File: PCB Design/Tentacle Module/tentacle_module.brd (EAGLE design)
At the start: 101.6 x 30.5 mm, 57 parts, among them IC1 OKR-T/10-W12, IC2 MC7805BDTRKG, IC3 UA78M33CKVU, T1 NTD5867NL, T2 NTD5867NL, T3 NTD5867NL, T4 NTD5867NL, X3 RJ45-8X, X5 RJ45-8X

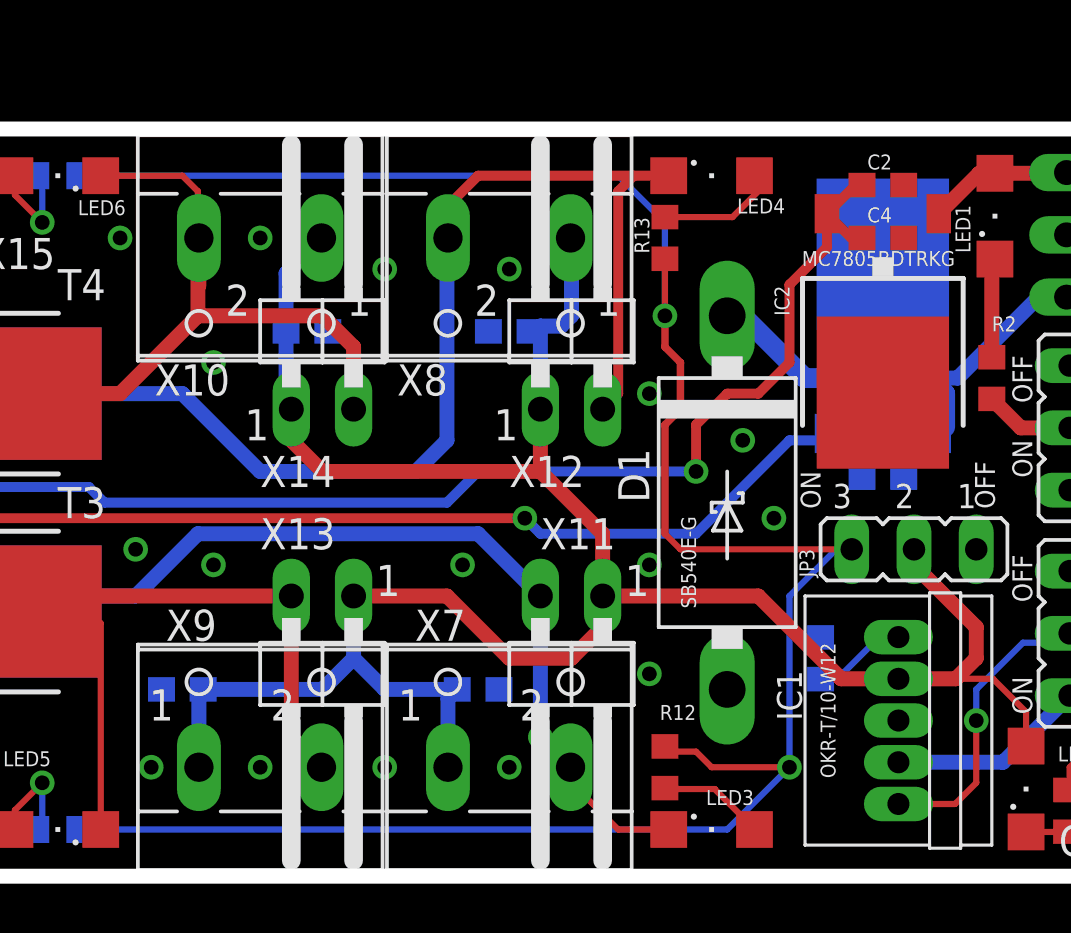
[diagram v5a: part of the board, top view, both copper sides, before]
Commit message: Changed 10uF caps package to 1206
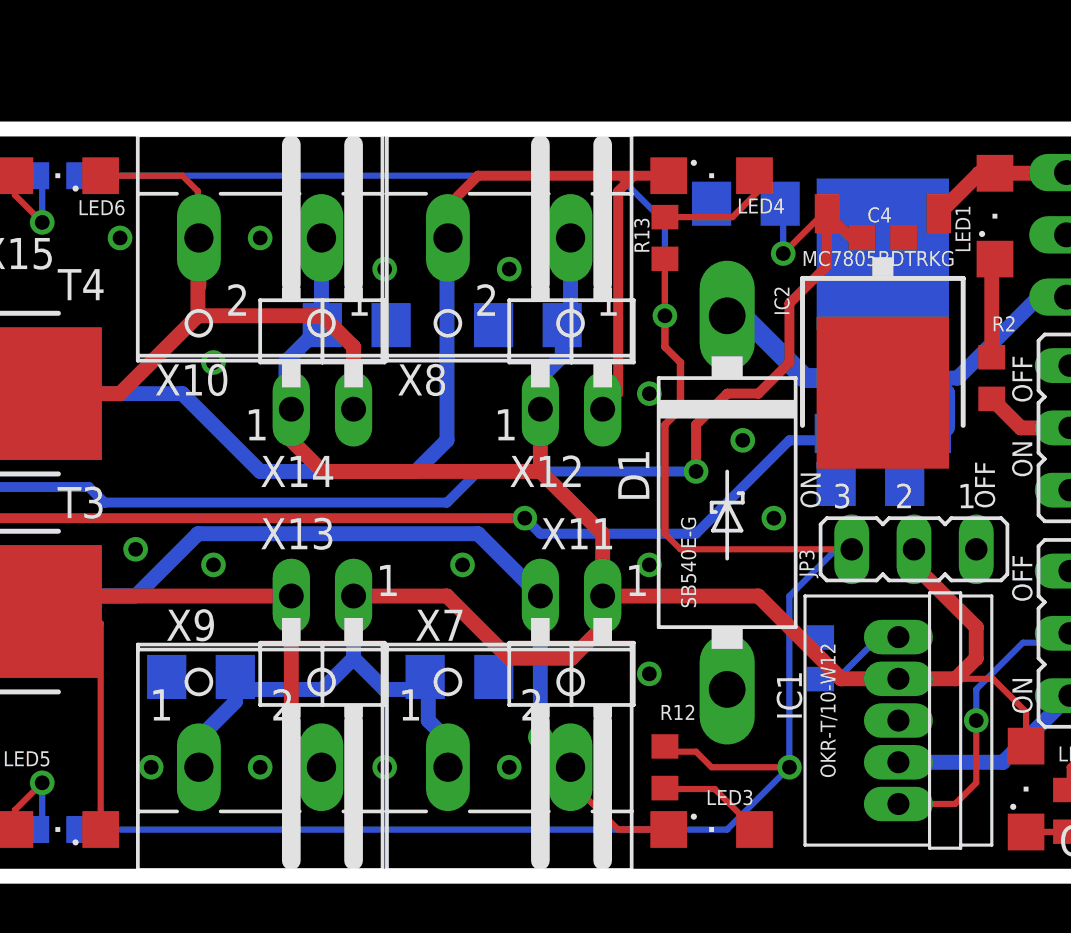
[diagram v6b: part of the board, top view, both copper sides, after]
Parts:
- C2, C3, C6, C7, C8, C9: device rcl:C0603 -> rcl:C1206
- moved C2 5.64 mm to (77.0, 27.4), flipped to the bottom
- moved C9 2.05 mm to (61.1, 22.5)
- moved C6 0.92 mm to (65.3, 8.13)
- moved C8 0.92 mm to (54.7, 8.13)
- moved C7 0.80 mm to (68.1, 22.5)
- moved C3 0.57 mm to (82.0, 16.0)
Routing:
- net +5V: track 101.6 -> 104.3 mm, vias 1 -> 2
- net +3.3V: track 69.9 -> 71.3 mm
- net +5V_HI-PWR: track 100.0 -> 98.5 mm

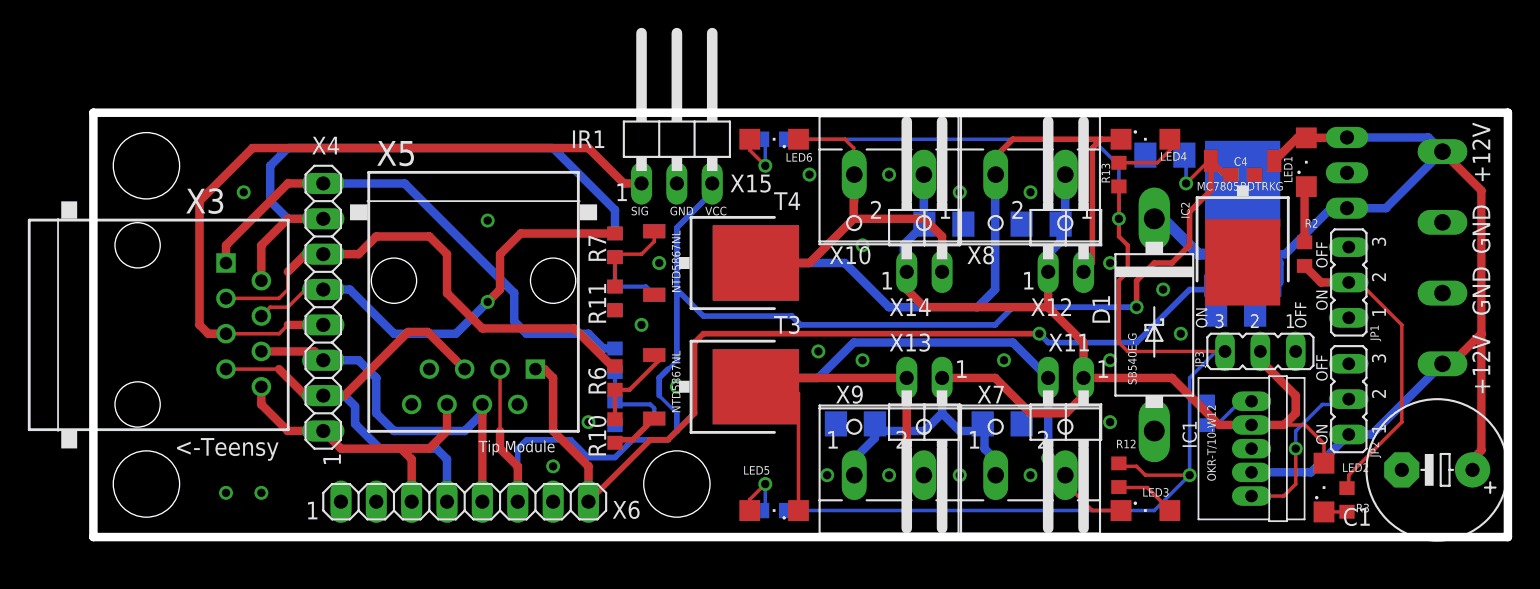
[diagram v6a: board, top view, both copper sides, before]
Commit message: Added labels to silkscreen
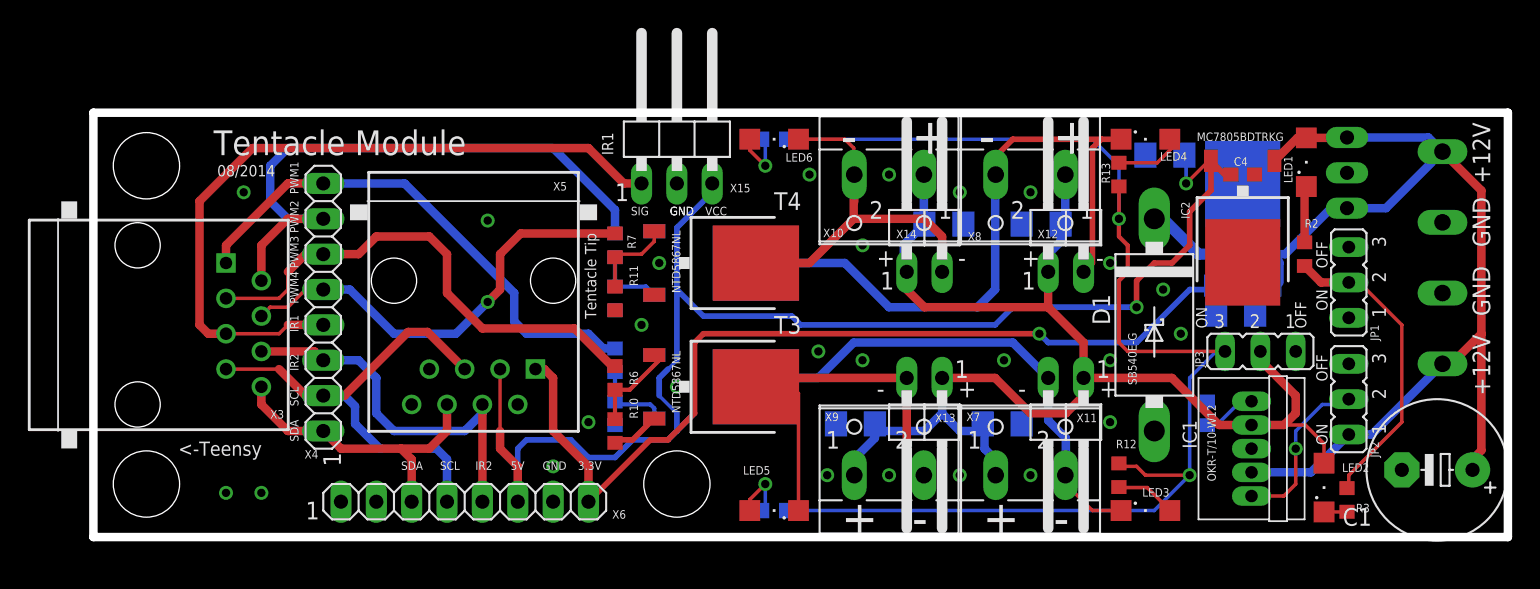
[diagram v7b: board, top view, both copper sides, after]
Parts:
- removed DRILEGEND: (no value), drilegend:DRILEGEND
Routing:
- net SMA1_OUT-: vias 1 -> 0
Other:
- board text added: "+"
- board text added: "-"
- board text added: "08/2014"
- board text added: "3.3V"
- board text added: "5V"
- board text added: "IR2"
- board text added: "PWM1"
- board text added: "PWM2"
- board text added: "PWM3"
- board text added: "PWM4"
- board text added: "SCL"
- board text added: "SDA"
- board text added: "Tentacle Module"
- board text added: "Tentacle Tip"
- board text removed: "Tip Module"
